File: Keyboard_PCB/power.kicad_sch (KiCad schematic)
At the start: 22 parts, among them U6 ISL91127IRAZ, U7 MCP73833

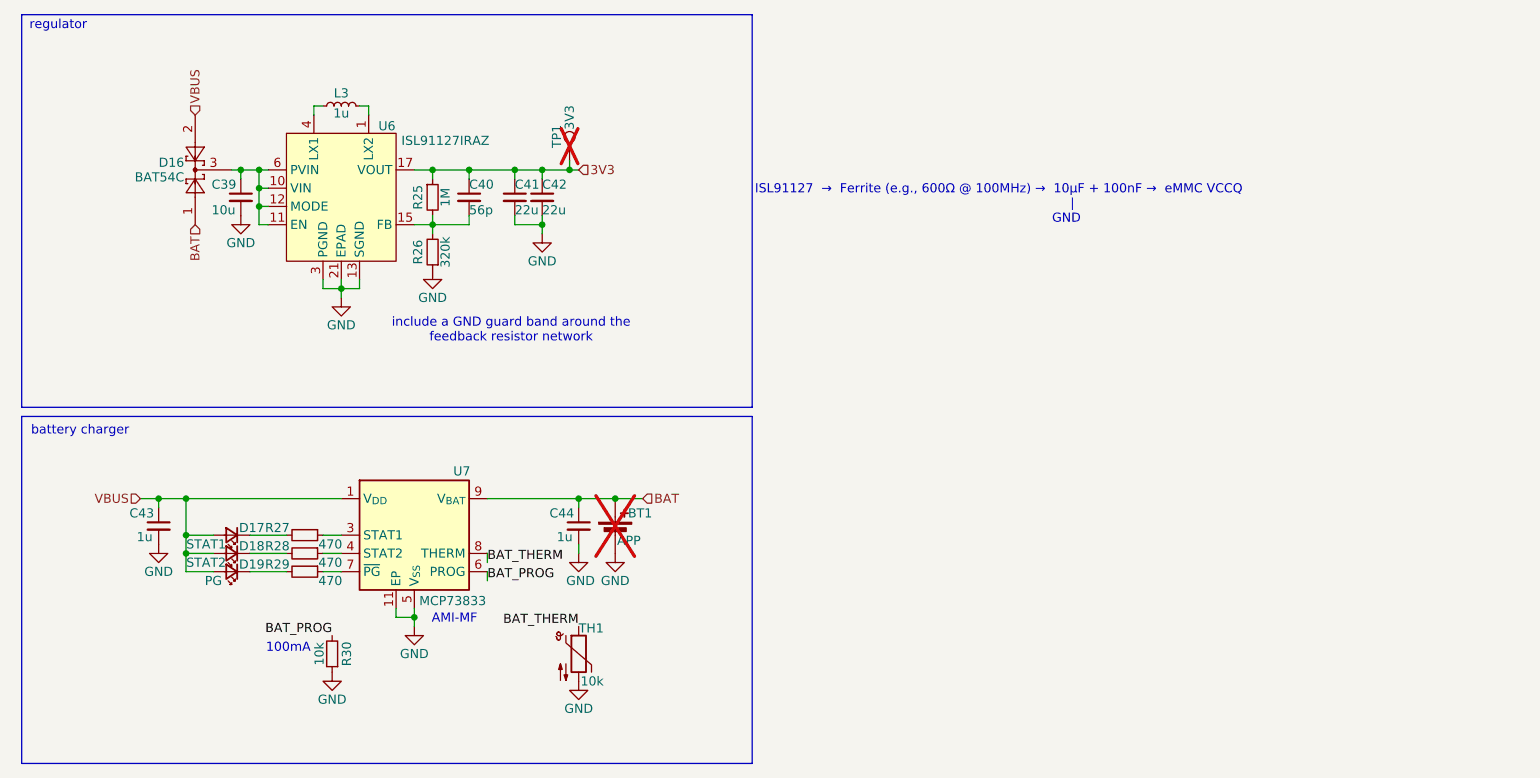
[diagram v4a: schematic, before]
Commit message: Added additional power filtering and improved RF path
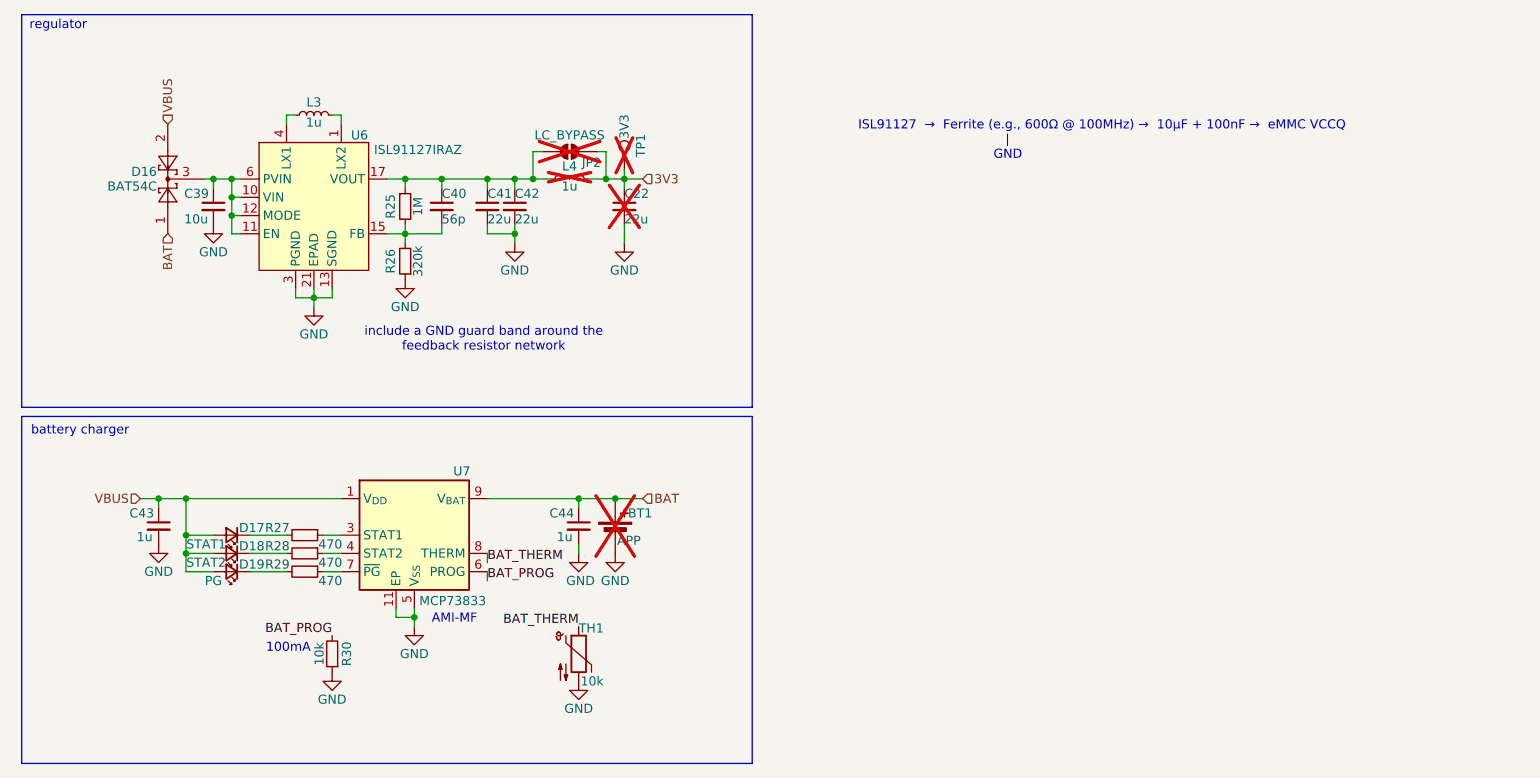
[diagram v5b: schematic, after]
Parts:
- added C22: 22u, Capacitor_SMD:C_0603_1608Metric, symbol Device:C_Small
- added JP2: LC_BYPASS, Jumper:SolderJumper-2_P1.3mm_Open_TrianglePad1.0x1.5mm, symbol Jumper:SolderJumper_2_Open
- added L4: 1u, Inductor_SMD:L_APV_ANR4018, symbol Device:L_Small
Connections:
- net 3V3: now also C22.1, JP2.2 (B), L4.2; no longer C40.1, C41.1, C42.1, R25.1, U6.17 (VOUT), U6.18 (VOUT), U6.19 (VOUT), U6.20 (VOUT)
- net GND: now also C22.2
- new net: C40.1, C41.1, C42.1, JP2.1 (A), L4.1, R25.1, U6.17 (VOUT), U6.18 (VOUT), U6.19 (VOUT), U6.20 (VOUT)
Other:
- moved on the sheet: C39, C40, C41, C42, D16, L3, R25, R26, TP1, U6

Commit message: Improved battery sens and added JLCPCB QR code
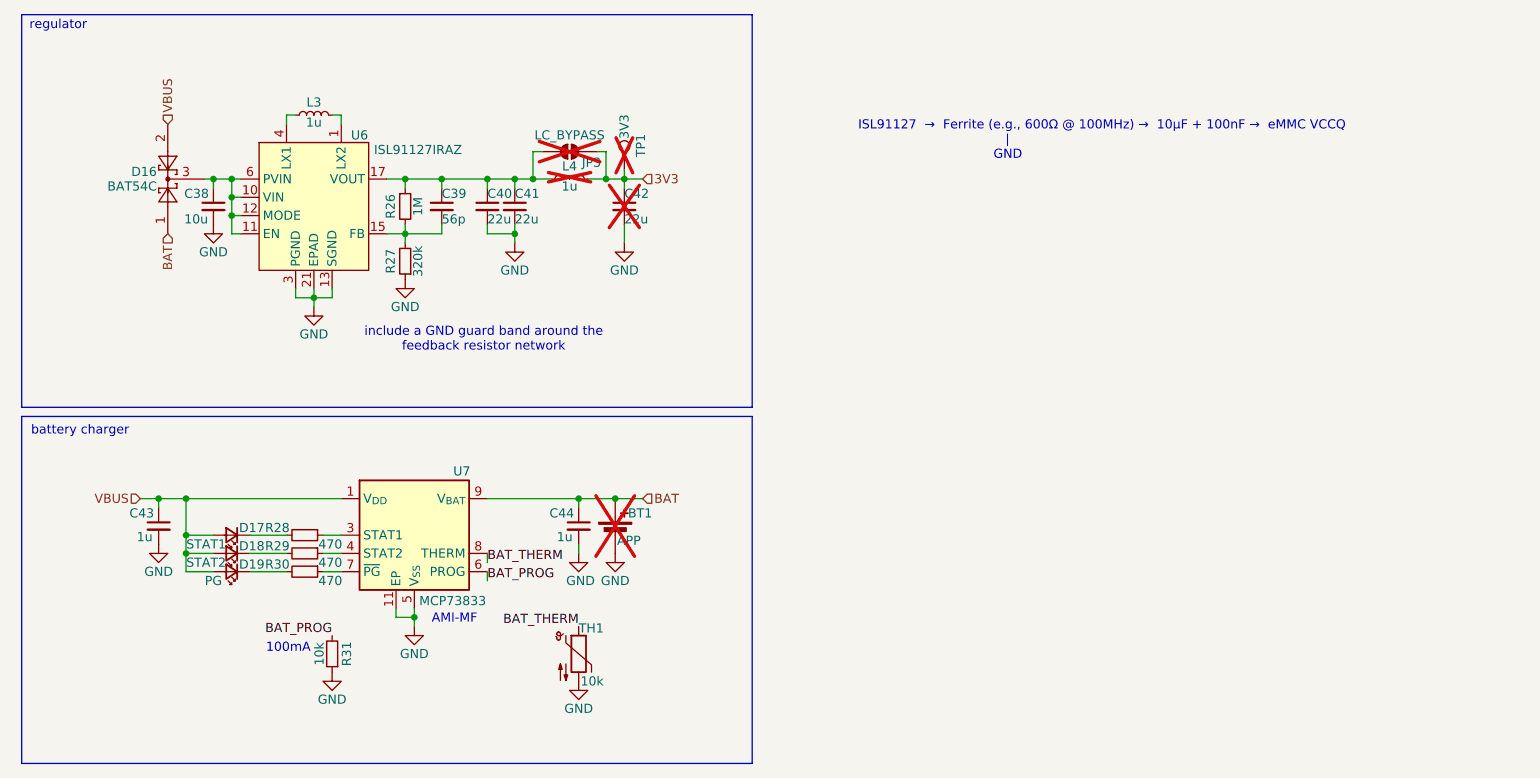
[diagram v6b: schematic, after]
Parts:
- renumbered C39 to C38, C40 to C39, C41 to C40, C42 to C41, C22 to C42, JP2 to JP3, R25 to R26, R26 to R27, R27 to R28, R28 to R29, R29 to R30, R30 to R31
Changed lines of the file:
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@@
 		(on_board yes)
 		(dnp yes)
-		(property "Reference" "JP2"
+		(property "Reference" "JP3"
 			(at 91.948 33.274 0)
 			(effects
@@
 			(project "Keyboard_PCB"
 				(path "/dd51e792-c76c-4d43-96de-494177f3b593/700844a0-d855-4a8d-a339-68e2adaa6562"
-					(reference "JP2")
+					(reference "JP3")
 					(unit 1)
 				)
@@
 		(on_board yes)
 		(dnp no)
-		(property "Reference" "C40"
+		(property "Reference" "C39"
 			(at 71.12 37.592 0)
 			(effects
@@
 			(project "Keyboard_PCB"
 				(path "/dd51e792-c76c-4d43-96de-494177f3b593/700844a0-d855-4a8d-a339-68e2adaa6562"
-					(reference "C40")
+					(reference "C39")
 					(unit 1)
 				)
@@
 		(on_board yes)
 		(dnp no)
-		(property "Reference" "#PWR081"
+		(property "Reference" "#PWR084"
 			(at 67.31 104.14 0)
 			(effects
@@
 			(project "Keyboard_PCB"
 				(path "/dd51e792-c76c-4d43-96de-494177f3b593/700844a0-d855-4a8d-a339-68e2adaa6562"
-					(reference "#PWR081")
+					(reference "#PWR084")
 					(unit 1)
 				)
@@
 		(on_board yes)
 		(dnp no)
-		(property "Reference" "C39"
+		(property "Reference" "C38"
 			(at 35.306 37.592 0)
 			(effects
@@
 			(project "Keyboard_PCB"
 				(path "/dd51e792-c76c-4d43-96de-494177f3b593/700844a0-d855-4a8d-a339-68e2adaa6562"
-					(reference "C39")
+					(reference "C38")
 					(unit 1)
 				)
@@
 		(on_board yes)
 		(dnp no)
-		(property "Reference" "R25"
+		(property "Reference" "R26"
 			(at 64.008 39.37 90)
 			(effects
@@
 			(project "Keyboard_PCB"
 				(path "/dd51e792-c76c-4d43-96de-494177f3b593/700844a0-d855-4a8d-a339-68e2adaa6562"
-					(reference "R25")
+					(reference "R26")
 					(unit 1)
 				)
@@
 		(on_board yes)
 		(dnp no)
-		(property "Reference" "R30"
+		(property "Reference" "R31"
 			(at 57.912 101.6 90)
 			(effects
@@
 			(project "Keyboard_PCB"
 				(path "/dd51e792-c76c-4d43-96de-494177f3b593/700844a0-d855-4a8d-a339-68e2adaa6562"
-					(reference "R30")
+					(reference "R31")
 					(unit 1)
 				)
@@
 		(on_board yes)
 		(dnp no)
-		(property "Reference" "R28"
+		(property "Reference" "R29"
 			(at 48.26 86.614 90)
 			(effects
@@
 			(project "Keyboard_PCB"
 				(path "/dd51e792-c76c-4d43-96de-494177f3b593/700844a0-d855-4a8d-a339-68e2adaa6562"
-					(reference "R28")
+					(reference "R29")
 					(unit 1)
 				)
@@
 		(on_board yes)
 		(dnp no)
-		(property "Reference" "#PWR078"
+		(property "Reference" "#PWR081"
 			(at 31.75 92.71 0)
 			(effects
@@
 			(project "Keyboard_PCB"
 				(path "/dd51e792-c76c-4d43-96de-494177f3b593/700844a0-d855-4a8d-a339-68e2adaa6562"
-					(reference "#PWR078")
+					(reference "#PWR081")
 					(unit 1)
 				)
@@
 		(on_board yes)
 		(dnp no)
-		(property "Reference" "#PWR083"
+		(property "Reference" "#PWR086"
 			(at 90.17 111.76 0)
 			(effects
@@
 			(project "Keyboard_PCB"
 				(path "/dd51e792-c76c-4d43-96de-494177f3b593/700844a0-d855-4a8d-a339-68e2adaa6562"
-					(reference "#PWR083")
+					(reference "#PWR086")
 					(unit 1)
 				)
@@
 		(on_board yes)
 		(dnp no)
-		(property "Reference" "R26"
+		(property "Reference" "R27"
 			(at 64.008 46.99 90)
 			(effects
@@
 			(project "Keyboard_PCB"
 				(path "/dd51e792-c76c-4d43-96de-494177f3b593/700844a0-d855-4a8d-a339-68e2adaa6562"
-					(reference "R26")
+					(reference "R27")
 					(unit 1)
 				)
@@
 		(on_board yes)
 		(dnp no)
-		(property "Reference" "#PWR074"
+		(property "Reference" "#PWR076"
 			(at 39.37 48.26 0)
 			(effects
@@
 			(project "Keyboard_PCB"
 				(path "/dd51e792-c76c-4d43-96de-494177f3b593/700844a0-d855-4a8d-a339-68e2adaa6562"
-					(reference "#PWR074")
+					(reference "#PWR076")
 					(unit 1)
 				)
@@
 		(on_board yes)
 		(dnp no)
-		(property "Reference" "C42"
+		(property "Reference" "C41"
 			(at 81.28 37.592 0)
 			(effects
@@
 			(project "Keyboard_PCB"
 				(path "/dd51e792-c76c-4d43-96de-494177f3b593/700844a0-d855-4a8d-a339-68e2adaa6562"
-					(reference "C42")
+					(reference "C41")
 					(unit 1)
 				)
@@
 		(on_board yes)
 		(dnp no)
-		(property "Reference" "#PWR080"
+		(property "Reference" "#PWR083"
 			(at 95.25 93.98 0)
 			(effects
@@
 			(project "Keyboard_PCB"
 				(path "/dd51e792-c76c-4d43-96de-494177f3b593/700844a0-d855-4a8d-a339-68e2adaa6562"
-					(reference "#PWR080")
+					(reference "#PWR083")
 					(unit 1)
 				)
@@
 		(on_board yes)
 		(dnp no)
-		(property "Reference" "R27"
+		(property "Reference" "R28"
 			(at 48.26 84.074 90)
 			(effects
@@
 			(project "Keyboard_PCB"
 				(path "/dd51e792-c76c-4d43-96de-494177f3b593/700844a0-d855-4a8d-a339-68e2adaa6562"
-					(reference "R27")
+					(reference "R28")
 					(unit 1)
 				)
@@
 		(on_board yes)
 		(dnp no)
-		(property "Reference" "C41"
+		(property "Reference" "C40"
 			(at 77.47 37.592 0)
 			(effects
@@
 			(project "Keyboard_PCB"
 				(path "/dd51e792-c76c-4d43-96de-494177f3b593/700844a0-d855-4a8d-a339-68e2adaa6562"
-					(reference "C41")
+					(reference "C40")
 					(unit 1)
 				)
@@
 		(on_board yes)
 		(dnp no)
-		(property "Reference" "#PWR076"
+		(property "Reference" "#PWR079"
 			(at 66.04 55.88 0)
 			(effects
@@
 			(project "Keyboard_PCB"
 				(path "/dd51e792-c76c-4d43-96de-494177f3b593/700844a0-d855-4a8d-a339-68e2adaa6562"
-					(reference "#PWR076")
+					(reference "#PWR079")
 					(unit 1)
 				)
@@
 		(on_board yes)
 		(dnp no)
-		(property "Reference" "#PWR077"
+		(property "Reference" "#PWR080"
 			(at 53.34 59.69 0)
 			(effects
@@
 			(project "Keyboard_PCB"
 				(path "/dd51e792-c76c-4d43-96de-494177f3b593/700844a0-d855-4a8d-a339-68e2adaa6562"
-					(reference "#PWR077")
+					(reference "#PWR080")
 					(unit 1)
 				)
@@
 		(on_board yes)
 		(dnp no)
-		(property "Reference" "R29"
+		(property "Reference" "R30"
 			(at 48.26 89.154 90)
 			(effects
@@
 			(project "Keyboard_PCB"
 				(path "/dd51e792-c76c-4d43-96de-494177f3b593/700844a0-d855-4a8d-a339-68e2adaa6562"
-					(reference "R29")
+					(reference "R30")
 					(unit 1)
 				)
@@
 		(on_board yes)
 		(dnp no)
-		(property "Reference" "#PWR085"
+		(property "Reference" "#PWR078"
 			(at 96.52 50.8 0)
 			(effects
@@
 			(project "Keyboard_PCB"
 				(path "/dd51e792-c76c-4d43-96de-494177f3b593/700844a0-d855-4a8d-a339-68e2adaa6562"
-					(reference "#PWR085")
+					(reference "#PWR078")
 					(unit 1)
 				)
@@
 		(on_board yes)
 		(dnp no)
-		(property "Reference" "#PWR079"
+		(property "Reference" "#PWR082"
 			(at 90.17 93.98 0)
 			(effects
@@
 			(project "Keyboard_PCB"
 				(path "/dd51e792-c76c-4d43-96de-494177f3b593/700844a0-d855-4a8d-a339-68e2adaa6562"
-					(reference "#PWR079")
+					(reference "#PWR082")
 					(unit 1)
 				)
@@
 		(on_board yes)
 		(dnp yes)
-		(property "Reference" "C22"
+		(property "Reference" "C42"
 			(at 96.52 37.592 0)
 			(effects
@@
 			(project "Keyboard_PCB"
 				(path "/dd51e792-c76c-4d43-96de-494177f3b593/700844a0-d855-4a8d-a339-68e2adaa6562"
-					(reference "C22")
+					(reference "C42")
 					(unit 1)
 				)
@@
 		(on_board yes)
 		(dnp no)
-		(property "Reference" "#PWR082"
+		(property "Reference" "#PWR085"
 			(at 55.88 110.49 0)
 			(effects
@@
 			(project "Keyboard_PCB"
 				(path "/dd51e792-c76c-4d43-96de-494177f3b593/700844a0-d855-4a8d-a339-68e2adaa6562"
-					(reference "#PWR082")
+					(reference "#PWR085")
 					(unit 1)
 				)
@@
 		(on_board yes)
 		(dnp no)
-		(property "Reference" "#PWR075"
+		(property "Reference" "#PWR077"
 			(at 81.28 50.8 0)
 			(effects
@@
 			(project "Keyboard_PCB"
 				(path "/dd51e792-c76c-4d43-96de-494177f3b593/700844a0-d855-4a8d-a339-68e2adaa6562"
-					(reference "#PWR075")
-					(unit 1)
-				)
+					(reference "#PWR077")
+					(unit 1)
+				)

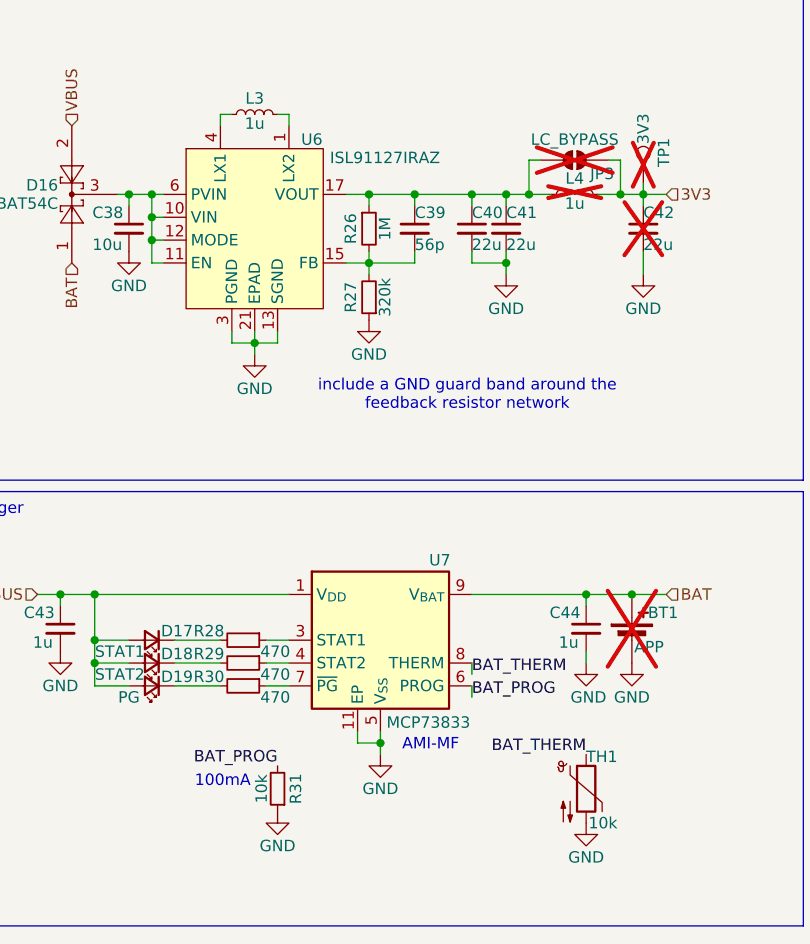
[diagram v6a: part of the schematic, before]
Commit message: Added active battery sensing circuit
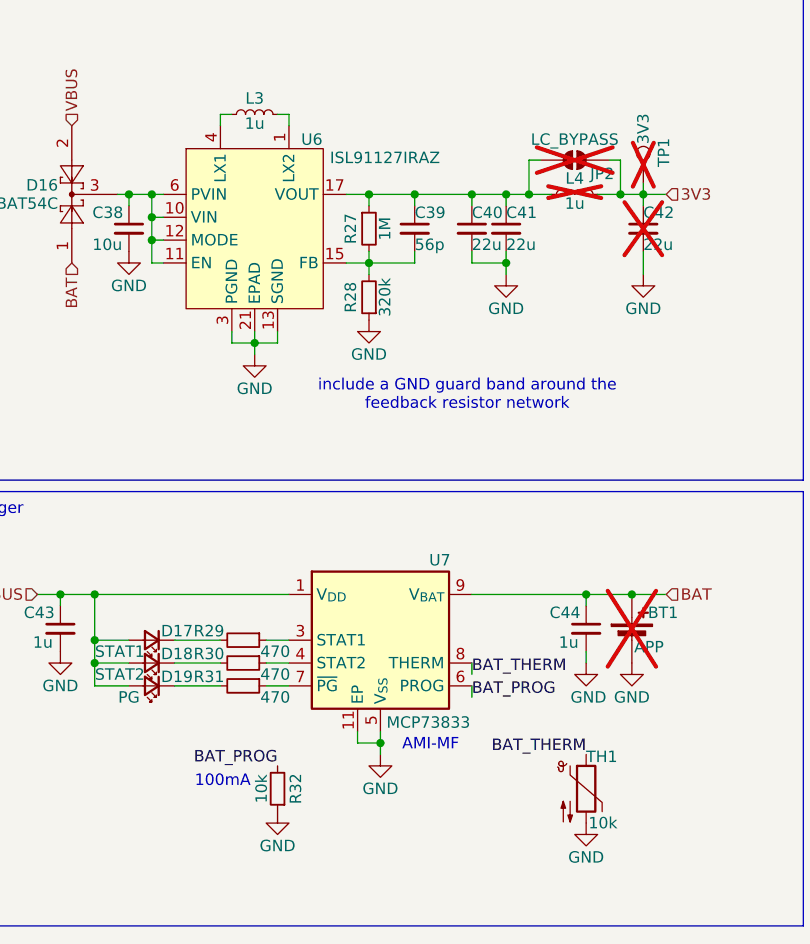
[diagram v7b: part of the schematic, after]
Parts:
- renumbered JP3 to JP2, R26 to R27, R27 to R28, R28 to R29, R29 to R30, R30 to R31, R31 to R32
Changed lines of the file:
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@@
 		(on_board yes)
 		(dnp yes)
-		(property "Reference" "JP3"
+		(property "Reference" "JP2"
 			(at 91.948 33.274 0)
 			(effects
@@
 			(project "Keyboard_PCB"
 				(path "/dd51e792-c76c-4d43-96de-494177f3b593/700844a0-d855-4a8d-a339-68e2adaa6562"
-					(reference "JP3")
+					(reference "JP2")
 					(unit 1)
 				)
@@
 		(on_board yes)
 		(dnp no)
-		(property "Reference" "R26"
+		(property "Reference" "R27"
 			(at 64.008 39.37 90)
 			(effects
@@
 			(project "Keyboard_PCB"
 				(path "/dd51e792-c76c-4d43-96de-494177f3b593/700844a0-d855-4a8d-a339-68e2adaa6562"
-					(reference "R26")
+					(reference "R27")
 					(unit 1)
 				)
@@
 		(on_board yes)
 		(dnp no)
-		(property "Reference" "R31"
+		(property "Reference" "R32"
 			(at 57.912 101.6 90)
 			(effects
@@
 			(project "Keyboard_PCB"
 				(path "/dd51e792-c76c-4d43-96de-494177f3b593/700844a0-d855-4a8d-a339-68e2adaa6562"
-					(reference "R31")
+					(reference "R32")
 					(unit 1)
 				)
@@
 		(on_board yes)
 		(dnp no)
-		(property "Reference" "R29"
+		(property "Reference" "R30"
 			(at 48.26 86.614 90)
 			(effects
@@
 			(project "Keyboard_PCB"
 				(path "/dd51e792-c76c-4d43-96de-494177f3b593/700844a0-d855-4a8d-a339-68e2adaa6562"
-					(reference "R29")
+					(reference "R30")
 					(unit 1)
 				)
@@
 		(on_board yes)
 		(dnp no)
-		(property "Reference" "R27"
+		(property "Reference" "R28"
 			(at 64.008 46.99 90)
 			(effects
@@
 			(project "Keyboard_PCB"
 				(path "/dd51e792-c76c-4d43-96de-494177f3b593/700844a0-d855-4a8d-a339-68e2adaa6562"
-					(reference "R27")
+					(reference "R28")
 					(unit 1)
 				)
@@
 		(on_board yes)
 		(dnp no)
-		(property "Reference" "R28"
+		(property "Reference" "R29"
 			(at 48.26 84.074 90)
 			(effects
@@
 			(project "Keyboard_PCB"
 				(path "/dd51e792-c76c-4d43-96de-494177f3b593/700844a0-d855-4a8d-a339-68e2adaa6562"
-					(reference "R28")
+					(reference "R29")
 					(unit 1)
 				)
@@
 		(on_board yes)
 		(dnp no)
-		(property "Reference" "R30"
+		(property "Reference" "R31"
 			(at 48.26 89.154 90)
 			(effects
@@
 			(project "Keyboard_PCB"
 				(path "/dd51e792-c76c-4d43-96de-494177f3b593/700844a0-d855-4a8d-a339-68e2adaa6562"
-					(reference "R30")
-					(unit 1)
-				)
+					(reference "R31")
+					(unit 1)
+				)
